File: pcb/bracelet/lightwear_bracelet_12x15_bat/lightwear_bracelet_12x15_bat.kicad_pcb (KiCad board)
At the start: 2 copper layers, 20.3 x 15.2 mm, 23 parts, among them Q1 NMOS, SW1 SW_SPST, U1 ATtiny1616-M, U2 WB6058D

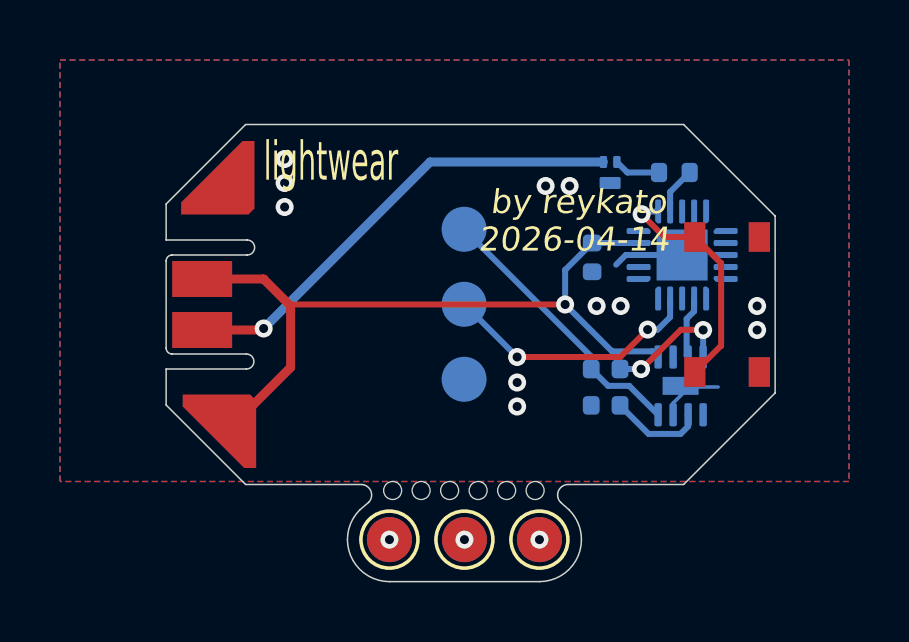
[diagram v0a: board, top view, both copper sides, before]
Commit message: fix footprint for sot-883 mosfet, add pads for flex button board
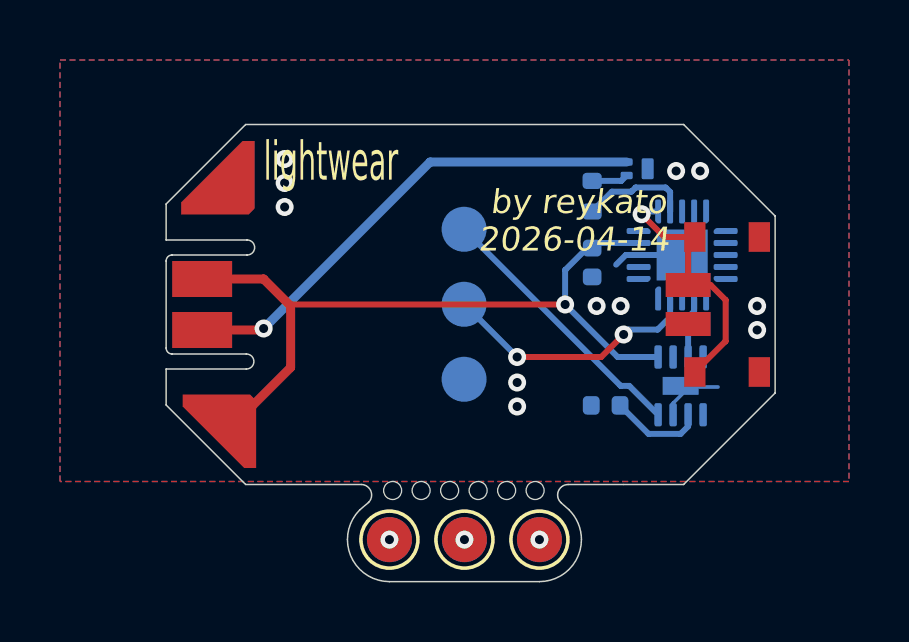
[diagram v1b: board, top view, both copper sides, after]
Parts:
- removed R1: 0R, Capacitor_SMD:C_0402_1005Metric
- added TP8: BTN, footprints:TestPoint_Pad_1.5x0.8mm_slim, F.Cu at (147.9, 91.5)
- added TP9: GND, footprints:TestPoint_Pad_1.5x0.8mm_slim, F.Cu at (147.9, 92.8)
- moved R3 2.85 mm to (144.7, 88.5), turned to 90 degrees
- moved Q1 0.91 mm to (146.2, 87.6), turned to 0 degrees
- moved C1 0.17 mm to (144.7, 90.8)
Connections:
- net Net-(SW1-B) renamed /BTN
- Q1 pad 1: /LEDK -> Net-(Q1-G)
- Q1 pad 2: Net-(Q1-G) -> /LEDK
- U2 pad 8: Net-(U2-EN) -> unconnected-(U2-EN-Pad8)
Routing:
- net Net-(U2-EN): track 4.22 -> 0.00 mm, vias 2 -> 0
- net Net-(U1-PA6): track 1.57 -> 3.64 mm
- net /LEDK: track 15.7 -> 16.5 mm
- net /BTN: track 8.13 -> 8.88 mm

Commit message: 12x15 bat PCB fixed with rev2 in code: removed references to onboard LED, restrict to only OFF, LOW, HIGH modes
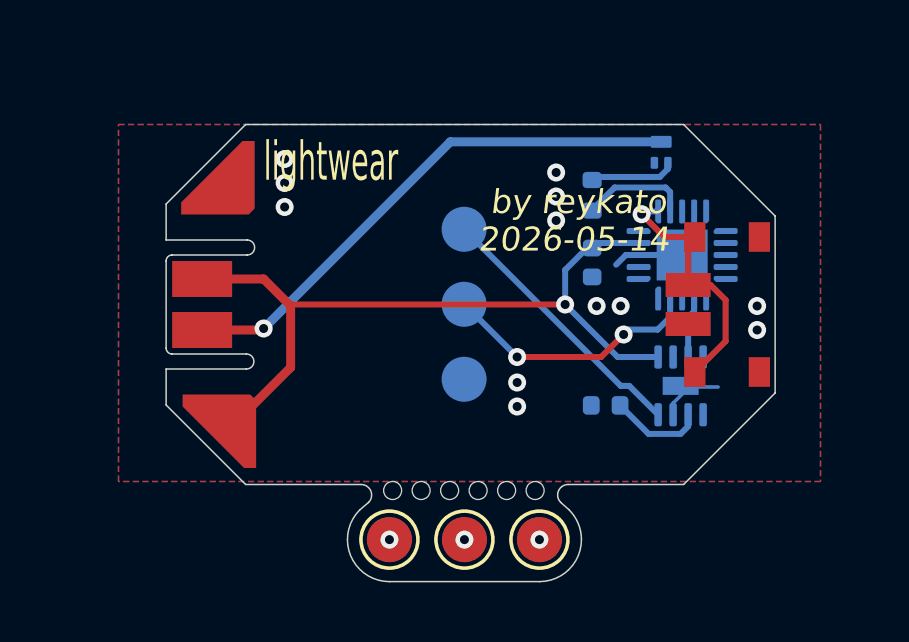
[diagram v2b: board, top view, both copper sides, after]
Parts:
- moved Q1 0.97 mm to (147.0, 87.1), turned to 90 degrees
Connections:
- Q1 pad 2: /LEDK -> GND
- Q1 pad 3: GND -> /LEDK
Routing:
- net Net-(Q1-G): track 1.22 -> 2.88 mm
- net /LEDK: track 16.5 -> 17.9 mm
- net GND: vias 11 -> 12
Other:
- board text added: "2026-05-14"
- board text removed: "2026-04-14"
